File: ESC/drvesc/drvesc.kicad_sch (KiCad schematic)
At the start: 25 parts, among them Q1 CSD18540Q5B, Q2 CSD18540Q5B, Q3 CSD18540Q5B, Q4 CSD18540Q5B, Q5 CSD18540Q5B, Q6 CSD18540Q5B, U1 DRV8305NPHP

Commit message: Feat[drvesc]: Began RP2040 control system
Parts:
- added JP1: RX, symbol Jumper:Jumper_2_Open
- added JP2: TX, symbol Jumper:Jumper_2_Open
- added TP1: ESC_PWM, symbol Connector:TestPoint_Small
- added TP2: ESC_RX, symbol Connector:TestPoint_Small
- added TP3: ESC_TX, symbol Connector:TestPoint_Small
- renumbered C2 to C1, C13 to C10, C17 to C11, C14 to C12, C18 to C13, C15 to C14, C12 to C2, C1 to C3, C9 to C4, C8 to C5, C10 to C6, C11 to C7, C7 to C8, C16 to C9
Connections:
- net EN_GATE: now reaches U1.1 (EN_GATE)
- net SDI: now reaches U1.10 (SDI)
- net SDO: now reaches U1.11 (SDO)
- net SCLK: now reaches U1.12 (SCLK)
- net PWRGD: now reaches U1.13 (PWRGD)
- net SO1: now reaches U1.16 (SO1)
- net SO2: now reaches U1.17 (SO2)
- net SO3: now reaches U1.18 (SO3)
- net INHA: now reaches U1.2 (INHA)
- net INLA: now reaches U1.3 (INLA)
- net INHB: now reaches U1.4 (INHB)
- net INLB: now reaches U1.5 (INLB)
- net INHC: now reaches U1.6 (INHC)
- net INLC: now reaches U1.7 (INLC)
- net NFAULT: now reaches U1.8 (NFAULT)
- net NSCS: now reaches U1.9 (NSCS)
- net +12V renamed PVDD
- new net BOARD_RX_1: JP1.1 (A)
- new net BOARD_TX_1: JP2.1 (A)
- new net ESC_PWM: TP1.1
- new net UART1_RX: JP1.2 (B), TP2.1
- new net UART1_TX: JP2.2 (B), TP3.1
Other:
- added sheet 5530843-7 (5530843-7.kicad_sch)
- added sheet RP2040 (RP2040.kicad_sch)
- note added: "Card Edge to ESC_Carrier"
- note added: "Control System"
- note added: "Half Bridges and Current Shunts"
- note removed: "MCU"
- note removed: "Power MOSFETs and Current Shunts"
- note removed: "copy byran prolly"
- moved on the sheet: C1, C2, C3, C4, C5, C6, C7, C8, R1, U1

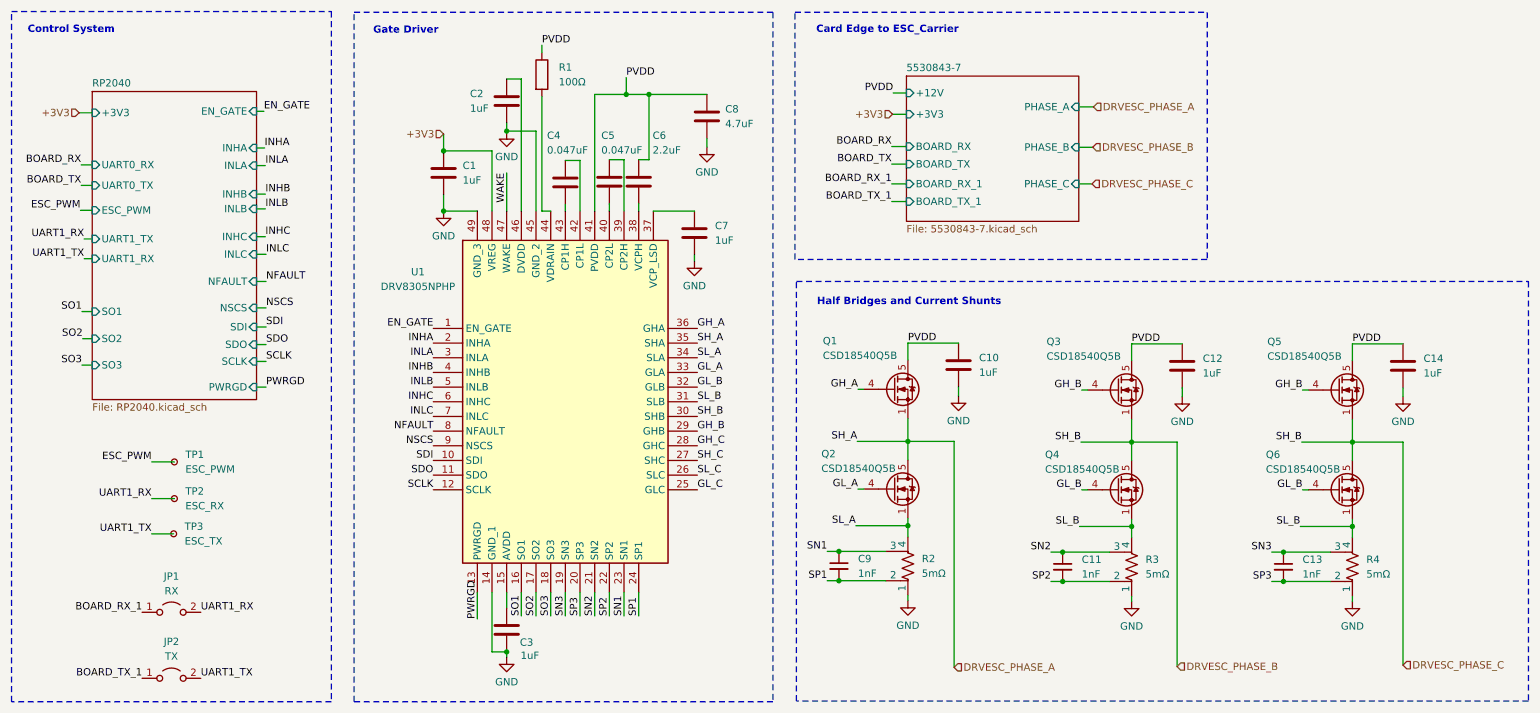
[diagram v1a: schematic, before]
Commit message: Feat: Finished RP2040 control system
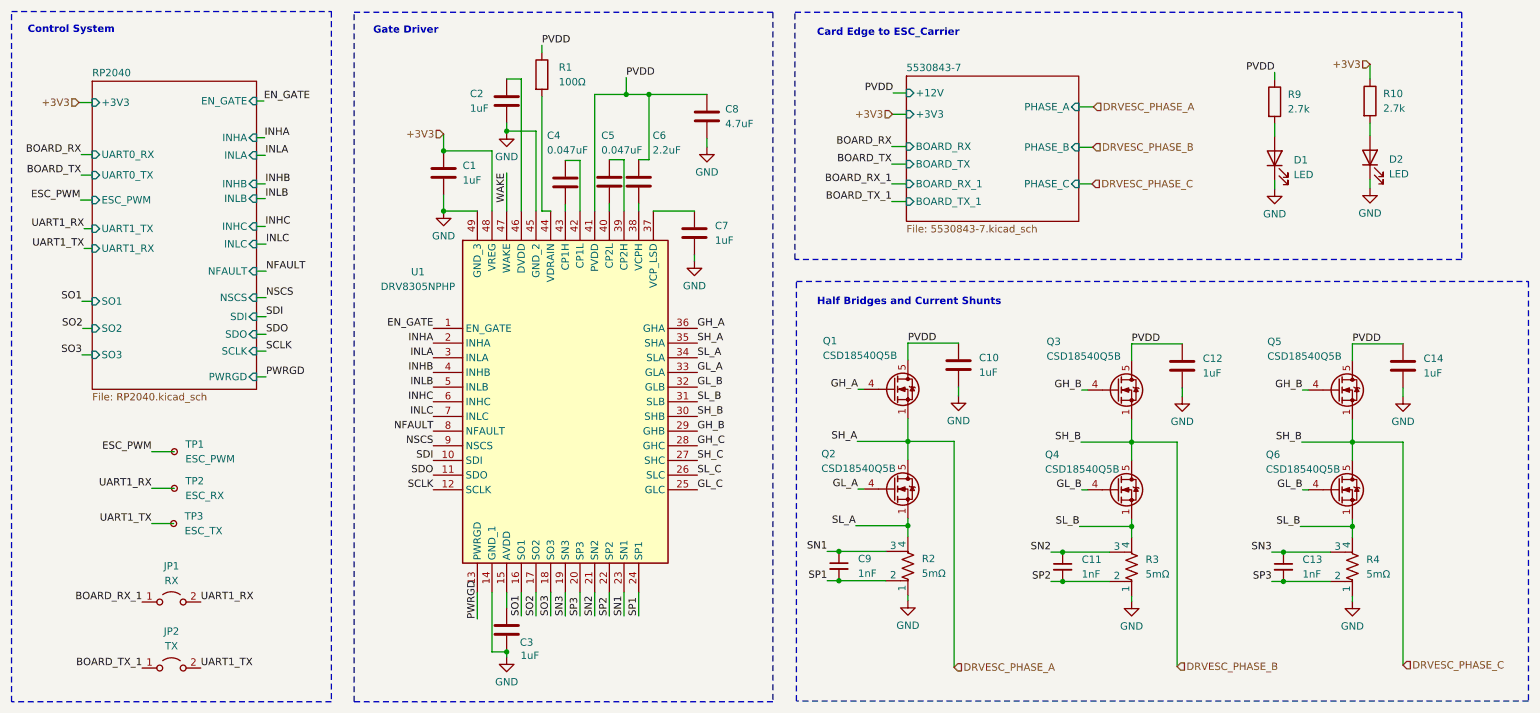
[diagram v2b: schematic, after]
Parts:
- added D1, D2: LED, symbol Device:LED
- added R10, R9: 2.7k, symbol Device:R
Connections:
- net +3V3: now also R10.1
- net GND: now also D1.1 (K), D2.1 (K)
- net PVDD: now also R9.1
- new net: D1.2 (A), R9.2
- new net: D2.2 (A), R10.2
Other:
- moved on the sheet: JP1, JP2, TP1, TP2, TP3

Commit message: Feat[drvesc]: Draft routing
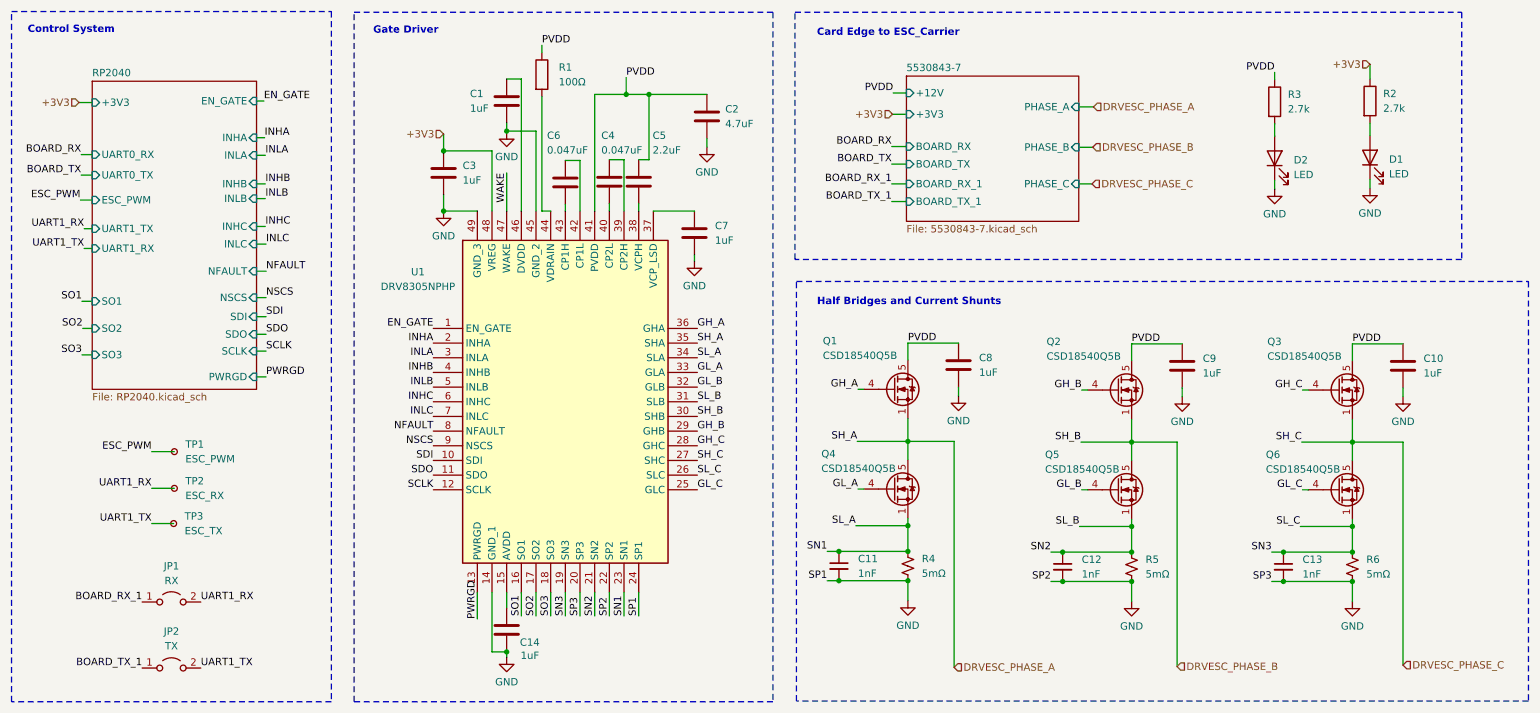
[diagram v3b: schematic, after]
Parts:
- removed R2, R3, R4: 5mΩ, symbol Device:R_Shunt_US
- added R4, R5, R6: 5mΩ, Resistor_SMD:R_2512_6332Metric, symbol Device:R_Small_US
- C1: renamed from C2; footprint (none) -> Capacitor_SMD:C_0603_1608Metric
- C10: renamed from C14; footprint (none) -> Capacitor_SMD:C_0603_1608Metric
- C11: renamed from C9; footprint (none) -> Capacitor_SMD:C_0603_1608Metric
- C12: renamed from C11; footprint (none) -> Capacitor_SMD:C_0603_1608Metric
- C13, C7: footprint (none) -> Capacitor_SMD:C_0603_1608Metric
- C14: renamed from C3; footprint (none) -> Capacitor_SMD:C_0603_1608Metric
- C2: renamed from C8; footprint (none) -> Capacitor_SMD:C_0603_1608Metric
- C3: renamed from C1; footprint (none) -> Capacitor_SMD:C_0603_1608Metric
- C4: renamed from C5; footprint (none) -> Capacitor_SMD:C_0603_1608Metric
- C5: renamed from C6; footprint (none) -> Capacitor_SMD:C_0603_1608Metric
- C6: renamed from C4; footprint (none) -> Capacitor_SMD:C_0603_1608Metric
- C8: renamed from C10; footprint (none) -> Capacitor_SMD:C_0603_1608Metric
- C9: renamed from C12; footprint (none) -> Capacitor_SMD:C_0603_1608Metric
- D1: renamed from D2; footprint (none) -> LED_SMD:LED_0603_1608Metric
- D2: renamed from D1; footprint (none) -> LED_SMD:LED_0603_1608Metric
- JP1, JP2: footprint (none) -> Jumper:SolderJumper-2_P1.3mm_Open_RoundedPad1.0x1.5mm
- R1: footprint (none) -> Resistor_SMD:R_0603_1608Metric
- R2: renamed from R10; footprint (none) -> Resistor_SMD:R_0603_1608Metric
- R3: renamed from R9; footprint (none) -> Resistor_SMD:R_0603_1608Metric
- TP1, TP2, TP3: footprint (none) -> Connector_PinHeader_2.54mm:PinHeader_1x01_P2.54mm_Vertical
- U1: footprint QFP50P900X900X120-49N -> DRV8305:QFP50P900X900X120-49N
- renumbered Q3 to Q2, Q5 to Q3, Q2 to Q4, Q4 to Q5
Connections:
- net SN1 is gone; now on net SL_A: C11.1, U1.23 (SN1)
- net SN2 is gone; now on net SL_B: C12.1, U1.21 (SN2)
- net SN3 is gone; now on net SL_C: C13.1, U1.19 (SN3)
- net SP1 is gone; now on net GND: C11.2, U1.24 (SP1)
- net SP2 is gone; now on net GND: C12.2, U1.22 (SP2)
- net SP3 is gone; now on net GND: C13.2, U1.20 (SP3)
- net DRVESC_PHASE_B: no longer Q3.1 (S), Q3.2 (S), Q3.3 (S), Q6.5 (D)
- net GH_B: no longer Q3.4 (G)
- net GH_C: now also Q3.4 (G)
- net GL_B: no longer Q6.4 (G)
- net GL_C: now also Q6.4 (G)
- net GND: now also R4.2, R5.2, R6.2
- net SL_A: now also R4.1
- net SL_B: now also R5.1; no longer Q6.1 (S), Q6.2 (S), Q6.3 (S)
- net SL_C: now also Q6.1 (S), Q6.2 (S), Q6.3 (S), R6.1
- net SH_C renamed DRVESC_PHASE_C
- net DRVESC_PHASE_C: now also Q3.1 (S), Q3.2 (S), Q3.3 (S), Q6.5 (D)

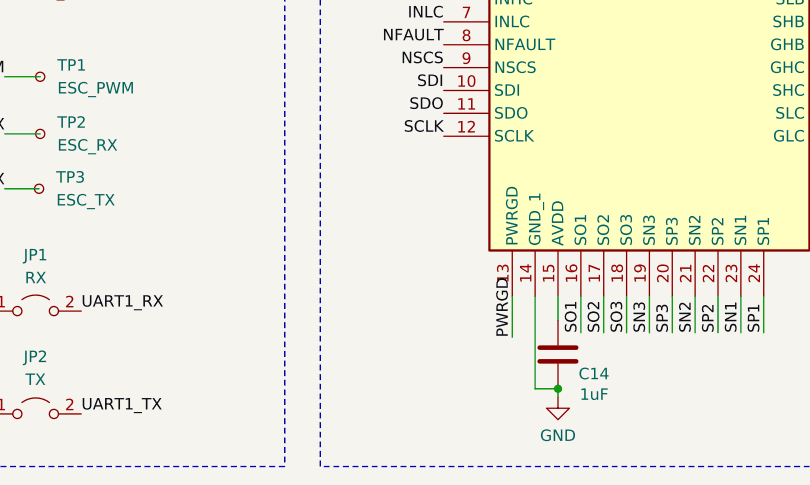
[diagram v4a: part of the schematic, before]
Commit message: Feat[drvesc]: Initial silkscreening
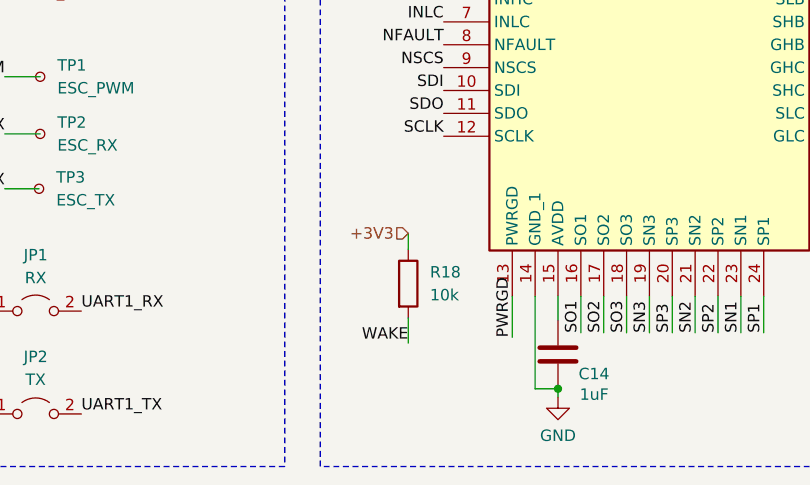
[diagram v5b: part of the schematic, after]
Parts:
- added R18: 10k, Resistor_SMD:R_0603_1608Metric, symbol Device:R
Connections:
- net +3V3: now also R18.1
- net WAKE: now also R18.2
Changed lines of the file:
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@@
+    (stroke (width 0) (type default))
+  )
+  (wire (pts (xy 86.487 135.001) (xy 86.487 136.779))
     (stroke (width 0) (type default))
   )
@@
   )
   (wire (pts (xy 113.284 74.803) (xy 113.284 75.946))
+    (stroke (width 0) (type default))
+  )
+  (wire (pts (xy 86.487 144.399) (xy 86.487 147.193))
     (stroke (width 0) (type default))
   )
@@
     (effects (font (size 1.27 1.27)) (justify left bottom))
   )
+  (label "WAKE" (at 86.487 147.193 180) (fields_autoplaced)
+    (effects (font (size 1.27 1.27)) (justify right bottom))
+  )
   (label "GH_A" (at 136.144 96.266 0) (fields_autoplaced)
     (effects (font (size 1.27 1.27)) (justify left bottom))
@@
   (hierarchical_label "DRVESC_PHASE_C" (shape input) (at 258.318 154.559 0) (fields_autoplaced)
     (effects (font (size 1.27 1.27)) (justify left))
+  )
+  (hierarchical_label "+3V3" (shape input) (at 86.487 135.001 180) (fields_autoplaced)
+    (effects (font (size 1.27 1.27)) (justify right))
   )
   (hierarchical_label "DRVESC_PHASE_A" (shape input) (at 204.724 57.912 0) (fields_autoplaced)
@@
         )
       )
+    )
+  )
+  (symbol (lib_id "Device:R") (at 86.487 140.589 0) (unit 1)
+    (in_bom yes) (on_board yes) (dnp no) (fields_autoplaced)
+    (property "Reference" "R18" (at 88.9 139.319 0)
+      (effects (font (size 1.27 1.27)) (justify left))
+    )
+    (property "Value" "10k" (at 88.9 141.859 0)
+      (effects (font (size 1.27 1.27)) (justify left))
+    )
+    (property "Footprint" "Resistor_SMD:R_0603_1608Metric" (at 84.709 140.589 90)
+      (effects (font (size 1.27 1.27)) hide)
+    )
+    (property "Datasheet" "~" (at 86.487 140.589 0)
+      (effects (font (size 1.27 1.27)) hide)
+    )
+    (pin "1")
+    (pin "2")
+    (instances
+      (project "drvesc"
+        (path "/98c2d148-7ff4-424c-a960-ad3471e42eda"
+          (reference "R18") (unit 1)
+        )
+      )
